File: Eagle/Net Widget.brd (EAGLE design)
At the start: 66 x 45.7 mm, 19 parts

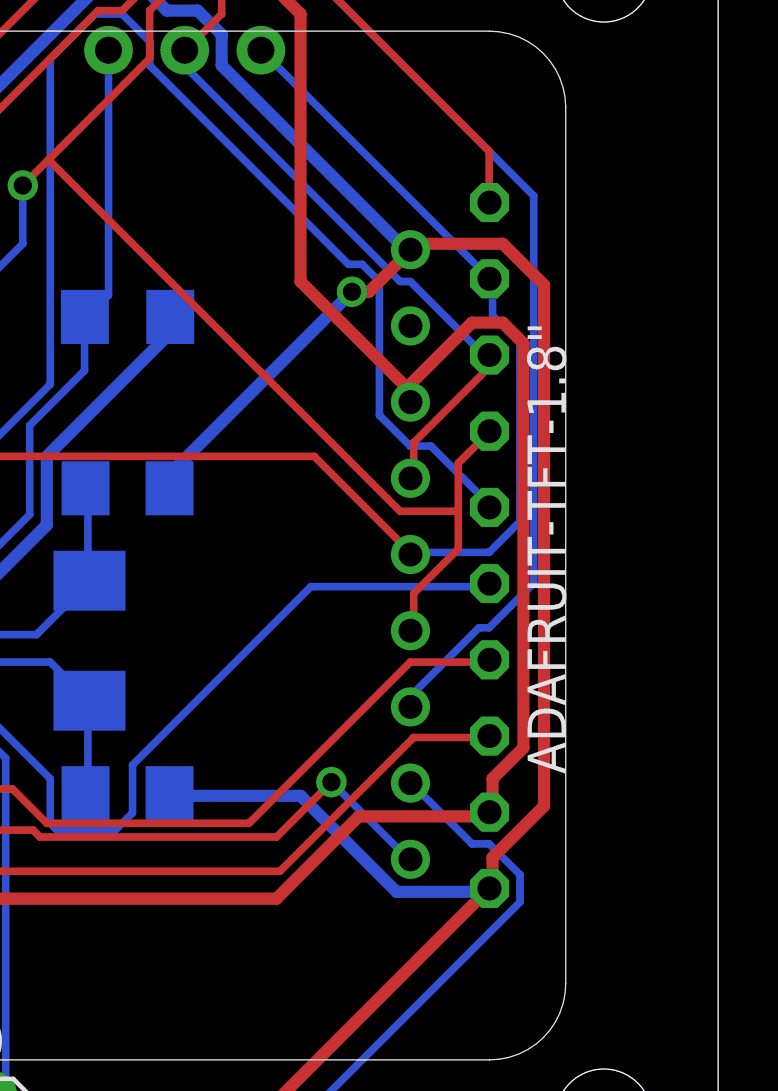
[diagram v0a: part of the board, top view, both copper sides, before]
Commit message: Switch to Net Widget.lbr and increase hole sizes.
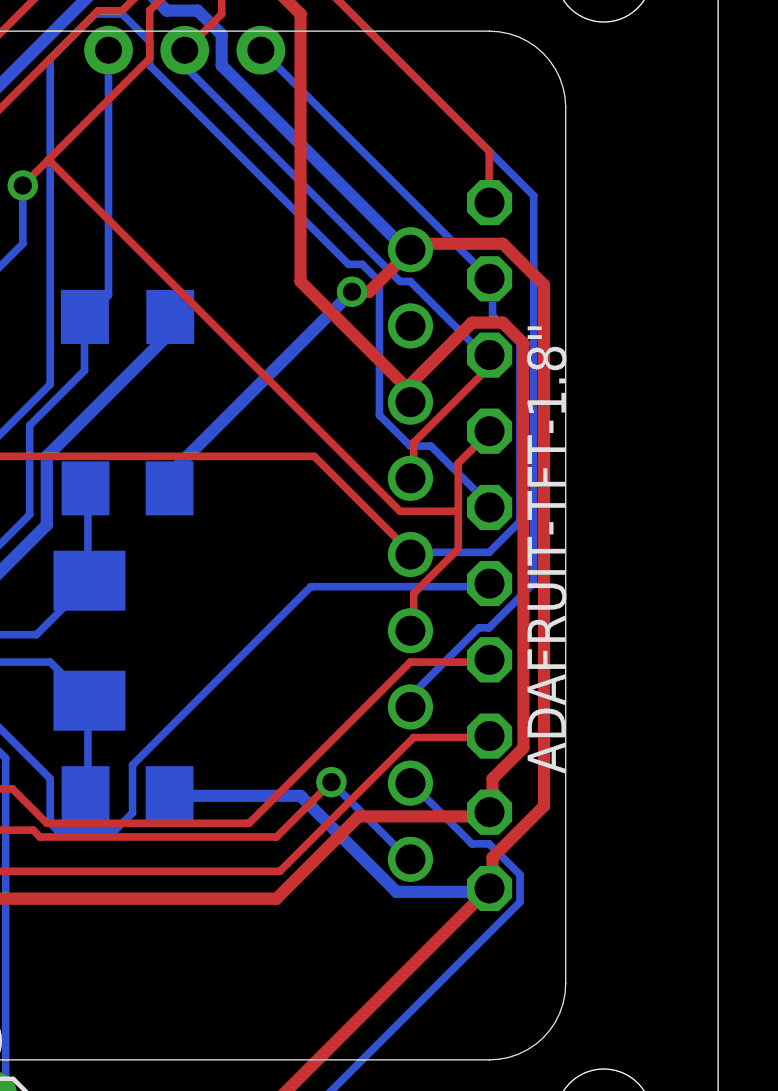
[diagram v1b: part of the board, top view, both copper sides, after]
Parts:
- U$2: device Weather Widget:ADAFRUIT-CC3000-BREAKOUT -> Net Widget:ADAFRUIT-CC3000-BREAKOUT
- U$3: device Weather Widget:ADAFRUIT-TFT1.8-BREAKOUT -> Net Widget:ADAFRUIT-TFT1.8-BREAKOUT
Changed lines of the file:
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@@
 <?xml version="1.0" encoding="utf-8"?>
 <!DOCTYPE eagle SYSTEM "eagle.dtd">
-<eagle version="7.1.0">
+<eagle version="7.2.0">
 <drawing>
 <settings>
@@
 <attribute name="VALUE" x="37.465" y="26.1699" size="1.27" layer="28" rot="MR0"/>
 </element>
-<element name="U$2" library="Weather Widget" package="ADAFRUIT-CC3000-BREAKOUT" value="ADAFRUIT-CC3000-BREAKOUT" x="57.785" y="35.56" rot="MR270"/>
-<element name="U$3" library="Weather Widget" package="ADAFRUIT-TFT1.8-BREAKOUT" value="ADAFRUIT-TFT1.8-BREAKOUT" x="33.02" y="22.86" rot="R180"/>
+<element name="U$2" library="Net Widget" package="ADAFRUIT-CC3000-BREAKOUT" value="ADAFRUIT-CC3000-BREAKOUT" x="57.785" y="35.56" rot="MR270"/>
+<element name="U$3" library="Net Widget" package="ADAFRUIT-TFT1.8-BREAKOUT" value="ADAFRUIT-TFT1.8-BREAKOUT" x="33.02" y="22.86" rot="R180"/>
 <element name="C4" library="rcl" package="C1206" value="10uF" x="19.05" y="22.86" smashed="yes" rot="MR270">
 <attribute name="NAME" x="17.78" y="24.13" size="1.27" layer="26" font="fixed" rot="MR270"/>

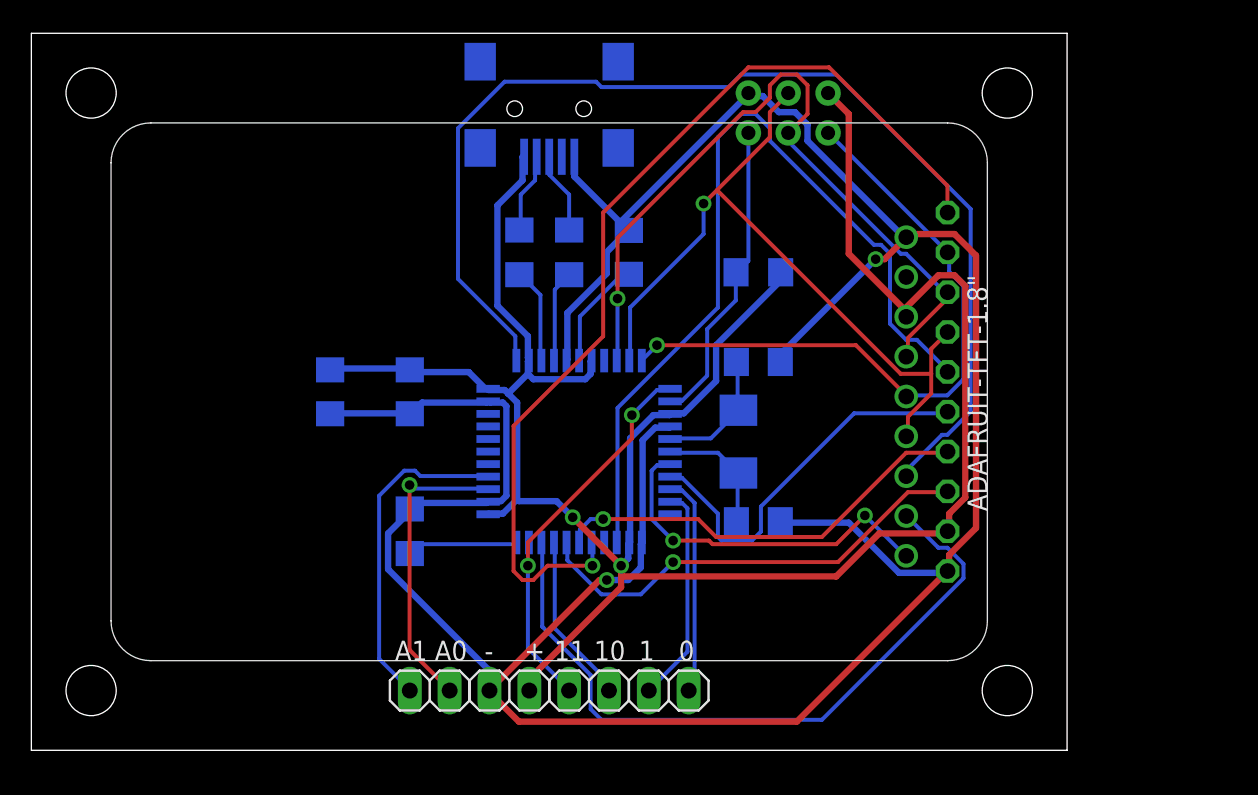
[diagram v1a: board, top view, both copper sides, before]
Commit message: Replace ATmega32U4 w/ ATmega1284P.
Initial pass. Adds an FTDI header and replaces the Mini-USB footprint.
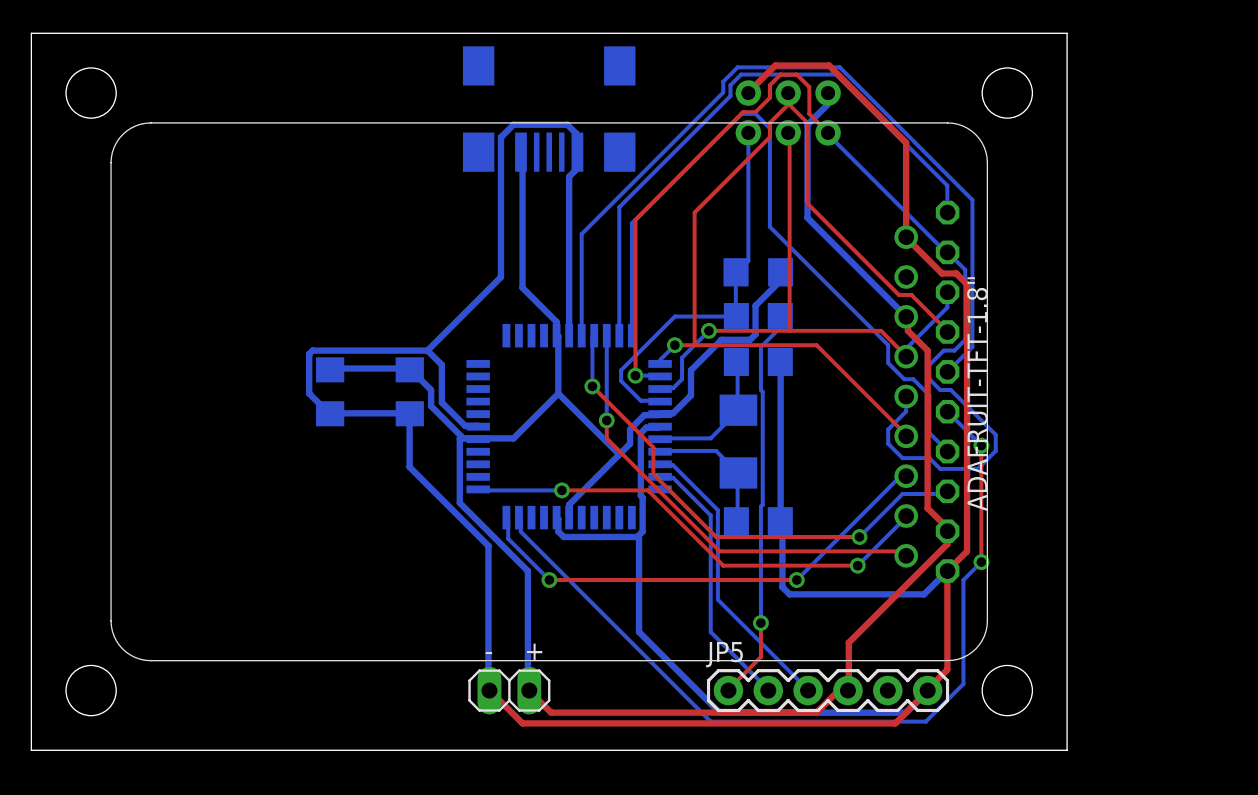
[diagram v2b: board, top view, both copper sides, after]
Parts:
- removed CN1: (no value), adafruit:USB-MINIB
- removed JP1, JP2, JP3: (no value), pinhead:1X02
- removed R1, R2: 22, rcl:R1206
- removed R3: 10K, rcl:R1206
- added IC1: MEGA164P/324P/644P-AU, avr-5:TQFP44
- added JP5: (no value), SparkFun-Connectors:1X06
- C1: value 1uF -> 0.1uF
- U$1: value ATMEGA32U4-AU -> USB_MINIB-POWER; device adafruit:TQFP44 -> Net Widget:USB_MINIB_POWER
- moved U$1 22.9 mm to (33.0, 41.9)
- moved C2 10.2 mm to (46.4, 14.6)
- moved C3 10.2 mm to (46.4, 24.8)
- moved C1 9.23 mm to (46.4, 27.6), turned to 180 degrees
- turned 16MHZ to 90 degrees
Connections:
- removed net D+: R1.2, U$1.4
- removed net D-: R2.2, U$1.3
- removed net D0: JP1.2, U$1.20
- removed net D1: JP1.1, U$1.21
- removed net D10: JP3.2, U$1.30
- removed net D11: JP3.1, U$1.12
- removed net N$2: CN1.D+, R1.1
- removed net N$3: CN1.D-, R2.1
- removed net N$4: C1.1, U$1.6
- removed net N$5: R3.1, U$1.33
- new net AREF: IC1.29
- new net N$1: C1.2, JP5.DTR
- new net RX: IC1.9, JP5.TXO
- new net TX: IC1.10, JP5.RXI
- net A0: now also IC1.37; no longer JP2.2, U$1.36
- net A1: now also IC1.36; no longer JP2.1, U$1.37
- net CARD_CS: now also IC1.21; no longer U$1.19
- net CS: now also IC1.22; no longer U$1.1
- net D/C: now also IC1.44; no longer U$1.28
- net GND: now also IC1.18, IC1.28, IC1.39, IC1.6, JP5.GND, U$1.GND; no longer C1.2, CN1.GND, R3.2, U$1.15, U$1.23, U$1.35, U$1.43, U$1.5
- net IRQ: now also IC1.42; no longer U$1.18
- net LITE: now also IC1.43; no longer U$1.27
- net MISO: now also IC1.2; no longer U$1.11
- net MOSI: now also IC1.1; no longer U$1.10
- net N$6: now also IC1.7; no longer U$1.17
- net N$7: now also IC1.8; no longer U$1.16
- net RESET: now also C1.1, IC1.4; no longer U$1.13
- net SCK: now also IC1.3; no longer U$1.9
- net TFT_CS: now also IC1.40; no longer U$1.25
- net TFT_RESET: now also IC1.41; no longer U$1.29
- net VBEN: now also IC1.23; no longer U$1.31
- net VCC: now also IC1.17, IC1.27, IC1.38, IC1.5, JP5.VCC, U$1.VBUS; no longer CN1.VBUS, U$1.14, U$1.2, U$1.24, U$1.34, U$1.44, U$1.7
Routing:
- net CS: track 73.3 -> 30.7 mm, vias 0 -> 2
- net GND: track 188.8 -> 225.6 mm, vias 2 -> 0
- net CARD_CS: track 24.6 -> 53.9 mm, vias 0 -> 2
- net MISO: track 42.1 -> 69.7 mm
- net LITE: track 63.0 -> 37.7 mm, vias 1 -> 0
- net N$1: track 0.00 -> 25.3 mm, vias 0 -> 1
- net D11: track 24.5 -> 0.00 mm, vias 2 -> 0
- net A1: track 21.0 -> 0.00 mm
- net A0: track 19.3 -> 0.00 mm, vias 1 -> 0
- net RX: track 0.00 -> 18.8 mm
- net D/C: track 27.3 -> 44.9 mm, vias 1 -> 0
- net TX: track 0.00 -> 16.9 mm
- net VBEN: track 45.5 -> 30.7 mm, vias 0 -> 2
- net D0: track 14.0 -> 0.00 mm
- net D1: track 13.9 -> 0.00 mm
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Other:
- board text added: "January 20, 2015"
- board text removed: "0"
- board text removed: "1"
- board text removed: "10"
- board text removed: "11"
- board text removed: "A0"
- board text removed: "A1"
- board text removed: "January 7, 2015"

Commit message: Clean up library and board.
Add breakout headers, move components into Net Widget library, switch
to Mini USB B connector with holes for mounting posts, silk screen
layout, etc.
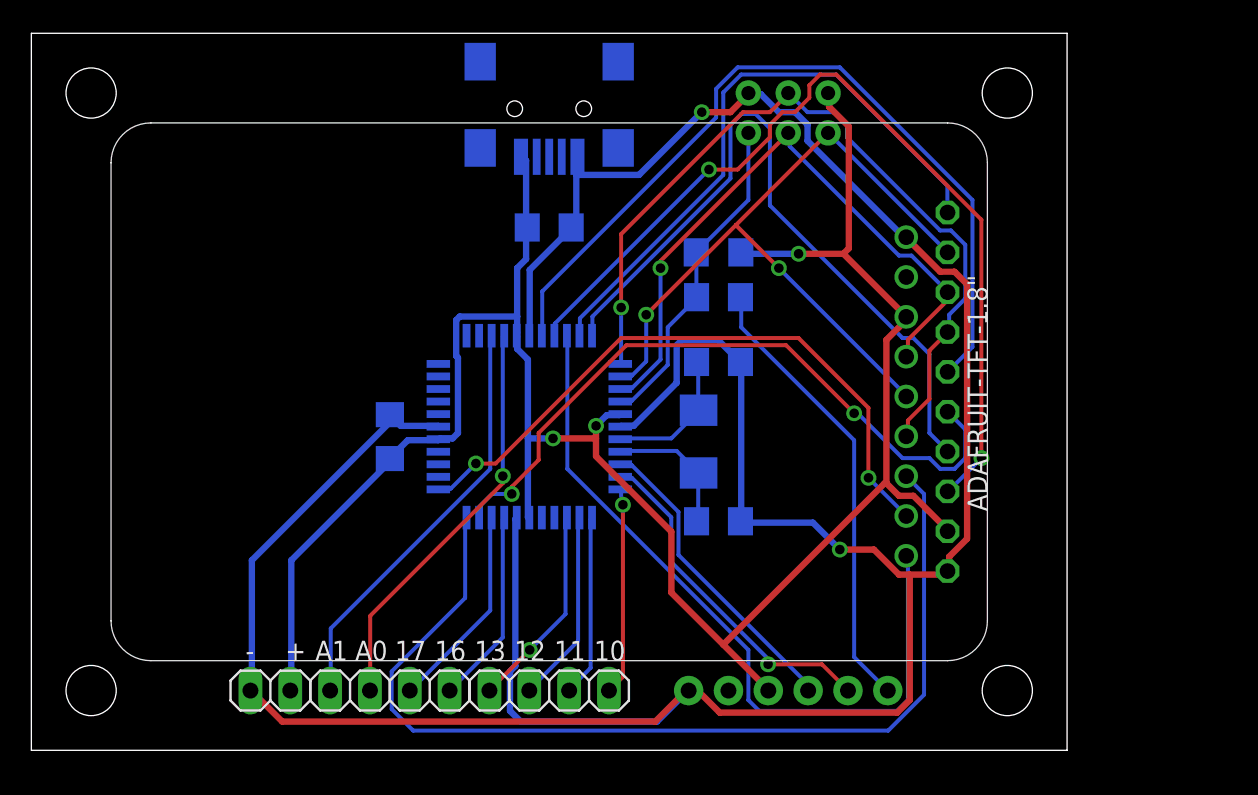
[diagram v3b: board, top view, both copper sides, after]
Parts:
- removed U$1: USB_MINIB-POWER, Net Widget:USB_MINIB_POWER
- added CN1: (no value), Net Widget:USB-MINIB-POWER
- added JP1: (no value), pinhead:1X04
- added JP2, JP3: (no value), pinhead:1X02
- 16MHZ: device fab:2-SMD-5X3MM -> Net Widget:2-SMD-5X3MM
- IC1: value MEGA164P/324P/644P-AU -> ATmega1284P
- JP5: value (none) -> FTDI; device SparkFun-Connectors:1X06 -> Net Widget:1X06
- moved C4 17.5 mm to (33.0, 33.3), turned to 180 degrees
- moved JP4 15.2 mm to (15.2, 3.81)
- moved JP5 10.2 mm to (54.6, 3.81), flipped to the bottom
- moved C5 3.13 mm to (22.9, 20.0), turned to 90 degrees
- moved C1 2.84 mm to (43.8, 28.9)
- moved R4 2.84 mm to (43.8, 31.8)
- moved 16MHZ 2.54 mm to (42.5, 19.7)
- moved C2 2.54 mm to (43.8, 14.6)
- moved C3 2.54 mm to (43.8, 24.8)
- moved IC1 2.54 mm to (31.8, 20.6)
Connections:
- net N$1 renamed DTR
- new net 10: IC1.11, JP1.1
- new net 11: IC1.12, JP1.2
- new net 12: IC1.13, JP1.3
- new net 13: IC1.14, JP1.4
- new net 16: IC1.19, JP3.1
- new net 17: IC1.20, JP3.2
- net A0: now also JP2.1
- net A1: now also JP2.2
- net GND: now also CN1.GND; no longer U$1.GND
- net VCC: now also CN1.VBUS; no longer U$1.VBUS
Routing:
- net CS: track 30.7 -> 64.1 mm, vias 2 -> 0
- net A1: track 0.00 -> 26.9 mm
- net A0: track 0.00 -> 26.2 mm, vias 0 -> 1
- net TFT_RESET: track 32.2 -> 57.6 mm
- net MISO: track 69.7 -> 47.6 mm, vias 1 -> 2
- net GND: track 225.6 -> 203.6 mm, vias 0 -> 2
- net IRQ: track 28.8 -> 48.0 mm, vias 1 -> 0
- net 10: track 0.00 -> 13.3 mm, vias 0 -> 1
- net 17: track 0.00 -> 13.2 mm
- net 13: track 0.00 -> 13.1 mm, vias 0 -> 1
- net 16: track 0.00 -> 12.5 mm
- net 12: track 0.00 -> 12.3 mm
- net 11: track 0.00 -> 11.6 mm
- net VBEN: track 30.7 -> 41.1 mm
- net CARD_CS: track 53.9 -> 44.2 mm
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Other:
- board text added: "10"
- board text added: "11"
- board text added: "12"
- board text added: "13"
- board text added: "16"
- board text added: "17"
- board text added: "A0"
- board text added: "A1"
- board text added: "B"
- board text added: "G"

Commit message: Replace TFT w/ temperature sensor.
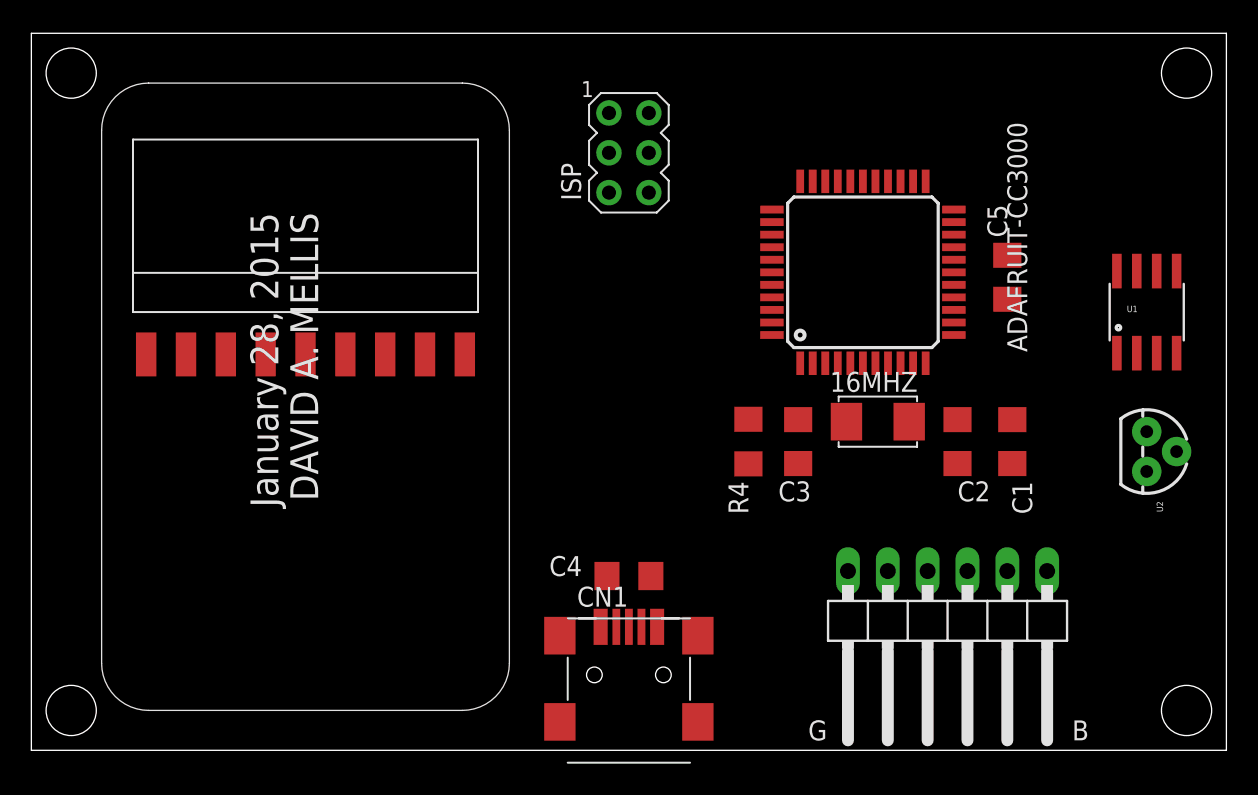
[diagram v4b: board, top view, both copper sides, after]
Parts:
- removed JP1: (no value), pinhead:1X04
- removed JP2, JP3, JP4: (no value), pinhead:1X02
- removed U$3: ADAFRUIT-TFT1.8-BREAKOUT, Net Widget:ADAFRUIT-TFT1.8-BREAKOUT
- added U1: (no value), Net Widget:SO08
- added U2: (no value), Net Widget:TO-92
- JP5: device Net Widget:1X06 -> Net Widget:1X06/90
- U$2: value ADAFRUIT-CC3000-BREAKOUT -> ADAFRUIT-CC3000-BREAKOUTRA; device Net Widget:ADAFRUIT-CC3000-BREAKOUT -> Net Widget:ADAFRUIT-CC3000-BREAKOUT-RA
- moved CN1 41.0 mm to (38.1, 2.54), flipped to the top, turned to 0 degrees
- moved C5 40.7 mm to (62.2, 30.2), flipped to the top
- moved U$2 28.2 mm to (30.5, 42.5), flipped to the top, turned to 180 degrees
- moved IC1 23.4 mm to (53.0, 30.5), flipped to the top, turned to 90 degrees
- moved C4 22.8 mm to (38.1, 11.1), flipped to the top, turned to 0 degrees
- moved C1 20.9 mm to (62.5, 19.7), flipped to the top, turned to 270 degrees
- moved C2 16.1 mm to (59.1, 19.7), flipped to the top, turned to 90 degrees
- moved R4 12.2 mm to (45.7, 19.7), flipped to the top, turned to 270 degrees
- moved 16MHZ 11.5 mm to (54.0, 21.0), flipped to the top, turned to 180 degrees
- moved ISP 10.5 mm to (38.1, 38.1), flipped to the top, turned to 0 degrees
- moved C3 7.18 mm to (48.9, 19.7), flipped to the top, turned to 90 degrees
- moved JP5 5.39 mm to (58.4, 7.62), flipped to the top, turned to 180 degrees
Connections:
- removed net 10: IC1.11, JP1.1
- removed net 11: IC1.12, JP1.2
- removed net 12: IC1.13, JP1.3
- removed net 13: IC1.14, JP1.4
- removed net 16: IC1.19, JP3.1
- removed net 17: IC1.20, JP3.2
- removed net A0: IC1.37, JP2.1
- removed net A1: IC1.36, JP2.2
- removed net CARD_CS: IC1.21, U$3.P$6
- removed net D/C: IC1.44, U$3.P$7
- removed net LITE: IC1.43, U$3.P$1
- removed net TFT_CS: IC1.40, U$3.P$5
- removed net TFT_RESET: IC1.41, U$3.P$8
- new net N$1: IC1.37, U1.1
- new net N$2: IC1.36, U2.2
- net 3V3: now also U$2.P$2; no longer U$2.P2
- net CS: now also U$2.P$7; no longer U$2.P7
- net DTR: now also JP5.6; no longer JP5.DTR
- net GND: now also JP5.1, U$2.P$1, U1.4, U2.3; no longer JP4.2, JP5.GND, U$2.P1, U$3.P$10
- net IRQ: now also U$2.P$9; no longer U$2.P9
- net MISO: now also U$2.P$5; no longer U$2.P5, U$3.P$2
- net MOSI: now also U$2.P$6; no longer U$2.P6, U$3.P$4
- net RX: now also JP5.4; no longer JP5.TXO
- net SCK: now also U$2.P$4; no longer U$2.P4, U$3.P$3
- net TX: now also JP5.5; no longer JP5.RXI
- net VBEN: now also U$2.P$8; no longer U$2.P8
- net VCC: now also JP5.3, U$2.P$3, U1.8, U2.1; no longer JP4.1, JP5.VCC, U$2.P3, U$3.P$9
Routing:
- net GND: track 203.6 -> 0.00 mm, vias 2 -> 0
- net VCC: track 139.4 -> 0.00 mm, vias 3 -> 0
- net CS: track 64.1 -> 0.00 mm
- net TFT_RESET: track 57.6 -> 0.00 mm, vias 2 -> 0
- net TFT_CS: track 52.4 -> 0.00 mm
- net MOSI: track 52.3 -> 0.00 mm, vias 1 -> 0
- net IRQ: track 48.0 -> 0.00 mm
- net MISO: track 47.6 -> 0.00 mm, vias 2 -> 0
- net D/C: track 46.0 -> 0.00 mm
- net CARD_CS: track 44.2 -> 0.00 mm, vias 2 -> 0
- net SCK: track 41.2 -> 0.00 mm, vias 1 -> 0
- net VBEN: track 41.1 -> 0.00 mm, vias 2 -> 0
- net LITE: track 38.7 -> 0.00 mm
- net DTR: track 29.0 -> 0.00 mm
- net A1: track 26.9 -> 0.00 mm
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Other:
- board size 66 x 45.7 mm -> 76.2 x 45.7 mm
- board text added: "January 28, 2015"
- board text removed: "+"
- board text removed: "-"
- board text removed: "10"
- board text removed: "11"
- board text removed: "12"
- board text removed: "13"
- board text removed: "16"
- board text removed: "17"
- board text removed: "A0"
- board text removed: "A1"
- board text removed: "ADAFRUIT-TFT-1.8""
- board text removed: "January 20, 2015"
